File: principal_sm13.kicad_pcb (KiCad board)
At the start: 2 copper layers, 82 parts, among them J1 CN_ARM, J2 CN_POLE, P12 CONN_10X2, P14 SPI, Q1 BC807, Q2 BC807, Q3 BC807, Q4 BC807, U1 L7812, U2 AD8397ARZ, U3 AD8397ARZ, X1 8.192MHz, X2 8.192MHz

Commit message: cambios en el placement
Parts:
- removed the C11 at (63.3, -95.7) (x3)
- removed the C12 at (63.3, -90.8) (x3)
- removed the C2 at (56.5, -71.0)
- removed the R1 at (63.3, -80.9) (x4)
- removed the R3 at (63.3, -85.8) (x3)
- removed the R4 at (63.3, -100.7) (x3)
- removed the U1 at (73.0, -66.5)
- added C27: 0,1µ, Capacitor_SMD:C_1206_3216Metric_Pad1.42x1.75mm_HandSolder, F.Cu at (56.5, -70.5)
- added R7: 1K, Resistor_SMD:R_1206_3216Metric_Pad1.42x1.75mm_HandSolder, F.Cu at (63.3, -80.9)
- added U3: L7812, Package_TO_SOT_THT:TO-218-3_Vertical, F.Cu at (73.0, -66.5)
- moved C13 0.27 mm to (56.5, -75.9)
- moved C7 0.27 mm to (49.0, -75.9)
- moved C12 0.10 mm to (56.5, -80.9)
- moved C6 0.10 mm to (49.0, -80.9)
- moved C19 0.07 mm to (-7.99, -81.1)
- renumbered C11 to C1, C8 to C10, C15 to C11, C9 to C12, C10 to C13, C24 to C14, C25 to C15, C26 to C16, C16 to C17, C19 to C18, C17 to C19, C12 to C2, C18 to C21, C21 to C22, C27 to C23, C22 to C24, C23 to C25, C1 to C26, C14 to C3, C3 to C4, C6 to C5, C4 to C6, C13 to C8, C5 to C9, P12 to P1, P14 to P2, R12 to R1, R11 to R10, R13 to R11, R20 to R12, R5 to R13, R15 to R14, R16 to R15, R17 to R16, R2 to R17, R14 to R18, R18 to R19, R4 to R2, R19 to R20, R6 to R3, R8 to R4, R9 to R5, R3 to R6, R7 to R8, R10 to R9, U2 to U1, U3 to U2

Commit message: componentes montados sobre placa CIAA NXP para hacer el sandwich
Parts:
- added F4: fiducial, Fiducial_1mm_BOT, F.Cu at (237.0, 104.0)
- added F5: fiducial, Fiducial_1mm_BOT, F.Cu at (120.6, 104.0)
- added F6: fiducial, Fiducial_1mm_BOT, F.Cu at (120.6, 180.5)
- P1, P2: moved to B.Cu
- moved J1 293.9 mm to (227.2, 103.9), turned to 180 degrees
- moved J2 293.9 mm to (170.7, 103.9), turned to 180 degrees
- moved P1 288.3 mm to (202.5, 147.7), turned to 270 degrees
- moved P2 282.0 mm to (157.7, 144.4)
- moved C27 276.0 mm to (239.1, 136.5), turned to 180 degrees
- moved C1 269.1 mm to (221.3, 122.1)
- moved C10 269.1 mm to (185.5, 127.3)
- moved C11 269.1 mm to (200.5, 117.3)
- moved C14 269.1 mm to (164.5, 122.1)
- moved C15 269.1 mm to (164.5, 127.0)
- moved C16 269.1 mm to (128.7, 117.3)
- moved C17 269.1 mm to (157.5, 112.3)
- moved C2 269.1 mm to (221.3, 127.0)
- moved C21 269.1 mm to (143.2, 127.3)
- moved C22 269.1 mm to (128.7, 127.3)
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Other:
- board outline added: 138.6 x 86.2 mm
- copper layers 2 -> 4
- net class Default: clearance 0.2 -> 0.2032; trace_width 0.25 -> 0.254; via_dia 0.8 -> 0.635; via_drill 0.4 -> 0.254
- net class POWER-IN added: clearance 0.2032, trace_width 0.762, via_dia 0.635, via_drill 0.254
- net class POWER-OUT added: clearance 0.2032, trace_width 0.508, via_dia 0.635, via_drill 0.254
- net class RS485-CAN added: clearance 0.254, trace_width 0.254, via_dia 0.635, via_drill 0.254
- net class Terminal Block added: clearance 0.2032, trace_width 0.508, via_dia 0.635, via_drill 0.254
- net class USB added: clearance 0.2032, trace_width 0.381, via_dia 0.635, via_drill 0.254
- rule pad_to_mask_clearance: 0 -> 0.0254
- rule trace_clearance: 0.2 -> 0.2032
- rule trace_min: 0.2 -> 0.254
- rule via_min_drill: 0.3 -> 0.254
- rule via_min_size: 0.4 -> 0.635
- board text added: "0 - 1 - 2 - 3 - 4 - 5 - 6 - 7"
- board text added: "1"
- board text added: "AUX"
- board text added: "CI"
- board text added: "CIAA-NXP"
- board text added: "DBG"
- board text added: "DIG. IN→"
- board text added: "DOUT"
- board text added: "DOUT |4|5|6|7|"
- board text added: "OTG"
- board text added: "PWR"
- board text added: "v1.0"
- board text added: "|"
- board text added: "|0|1|2|3|"

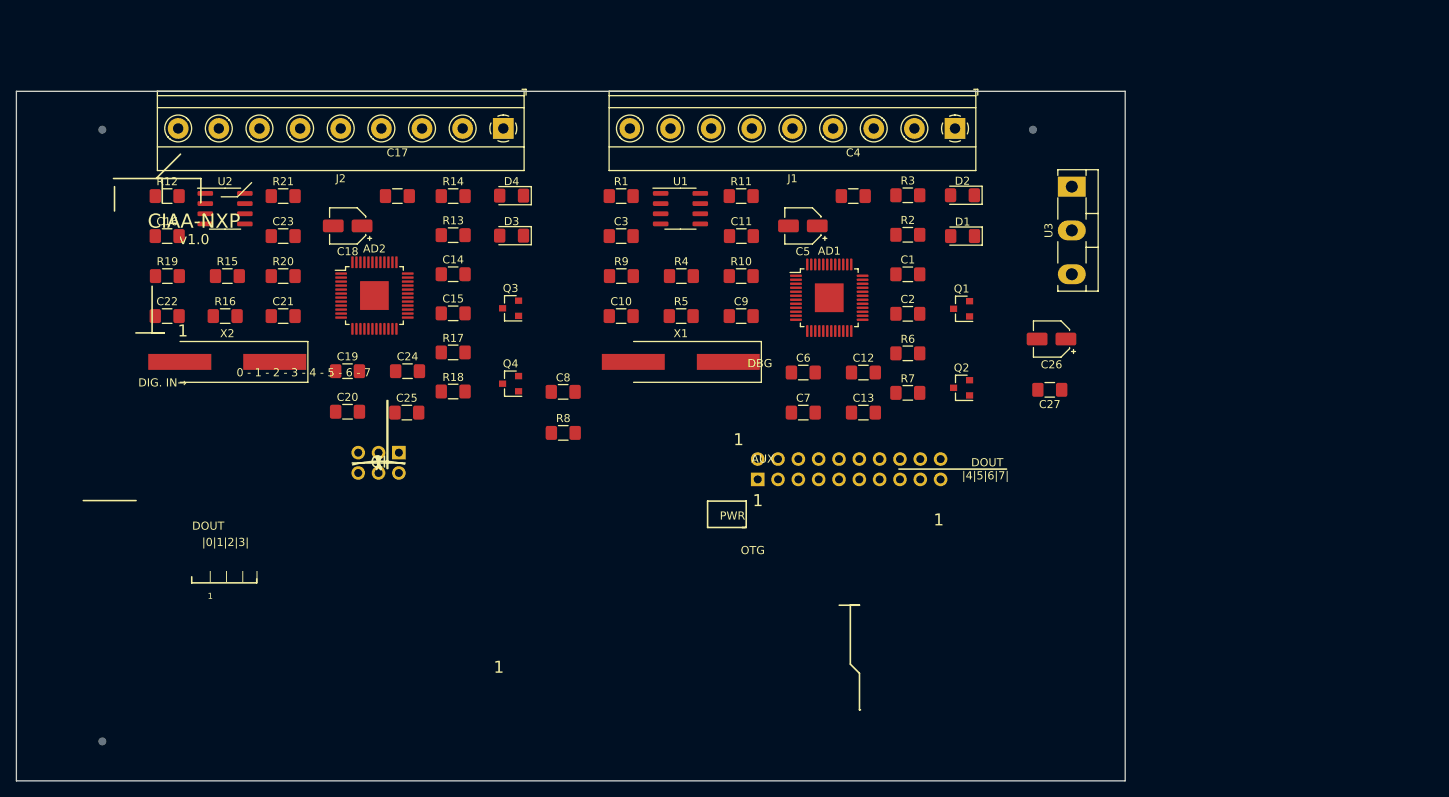
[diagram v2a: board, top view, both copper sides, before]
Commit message: reubicados componentes, cambiado regulador a SMD
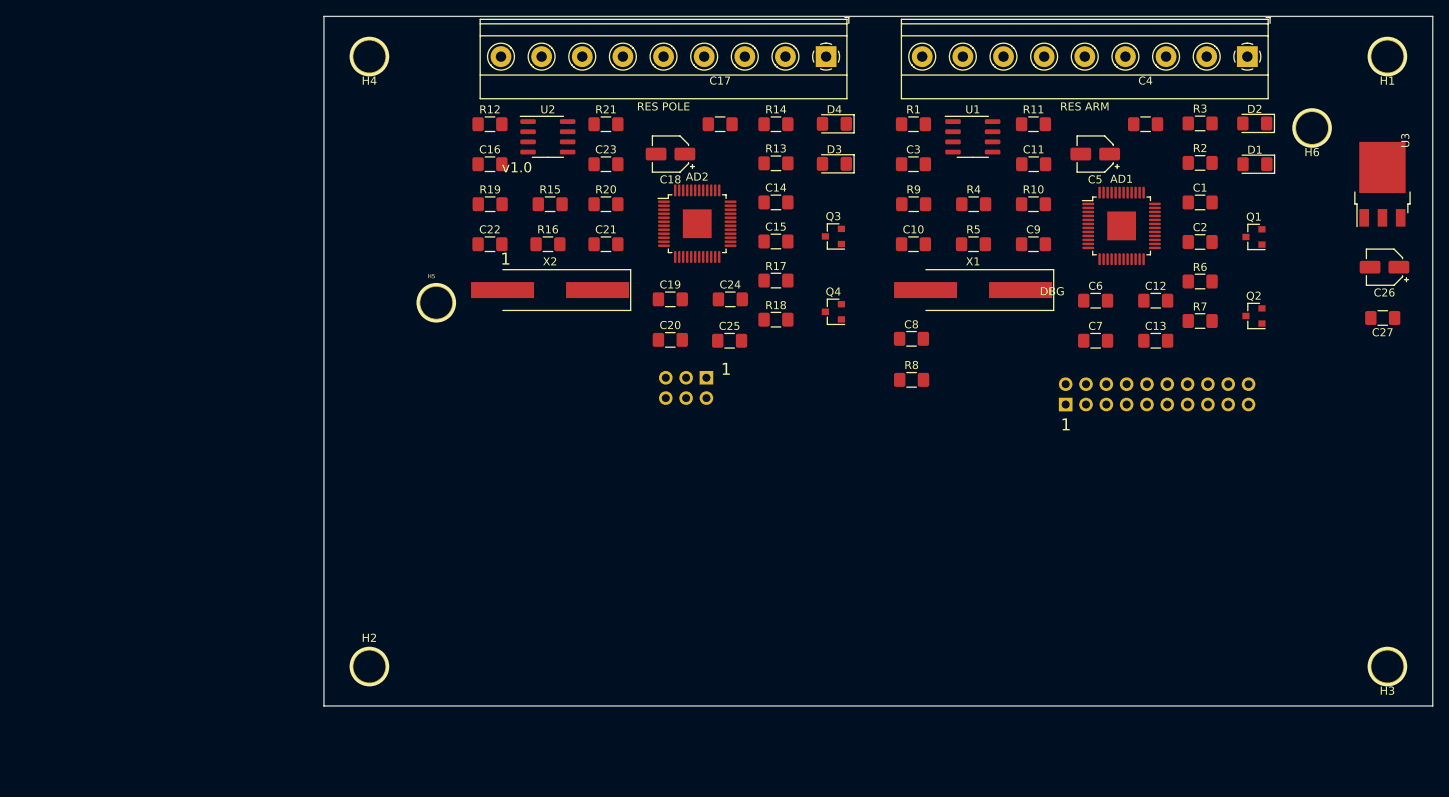
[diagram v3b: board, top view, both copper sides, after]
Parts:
- removed F4, F5, F6: fiducial, Fiducial_1mm_BOT
- removed P2: SPI, Connector_PinSocket_2.54mm:PinSocket_2x03_P2.54mm_Vertical
- added ?: , , F.Cu at (463.9, 242.3)
- added H1: 4mm, 1pin, F.Cu at (281.3, 94.9)
- added H2: 4mm, 1pin, F.Cu at (154.0, 171.1)
- added H3: 4mm, 1pin, F.Cu at (281.3, 171.1)
- added H4: 4mm, 1pin, F.Cu at (154.0, 94.9)
- added H5: 4mm, 1pin, F.Cu at (162.4, 125.6)
- added H6: 4mm, 1pin, F.Cu at (271.8, 103.8)
- added SPI: SPI, Connector_PinSocket_2.54mm:PinSocket_2x03_P2.54mm_Vertical, B.Cu at (196.1, 135.0)
- RES ARM: renamed from J1
- RES POLE: renamed from J2
- U3: footprint Package_TO_SOT_THT:TO-218-3_Vertical -> Package_TO_SOT_SMD:TO-252-3_TabPin2
- moved C8 44.0 mm to (221.8, 130.2)
- moved R8 44.0 mm to (221.8, 135.3)
- moved C27 42.6 mm to (280.7, 127.5)
- moved C26 42.6 mm to (280.9, 121.2)
- moved C17 41.3 mm to (197.9, 103.3)
- moved C25 41.3 mm to (199.0, 130.4)
- moved D3 41.3 mm to (212.1, 108.3)
- moved D4 41.3 mm to (212.1, 103.3)
- moved R15 41.3 mm to (176.6, 113.3)
- moved R19 41.3 mm to (169.1, 113.3)
- moved R18 41.3 mm to (204.8, 127.8)
- moved AD2 41.3 mm to (195.0, 115.8)
- moved C14 41.3 mm to (204.8, 113.1)
- moved C15 41.3 mm to (204.8, 118.0)
- moved C16 41.3 mm to (169.1, 108.3)
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- renumbered P1 to GPIO
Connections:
- AD1 pad 14: Net-(AD1-Pad14) -> (no net)
- AD1 pad 15: Net-(AD1-Pad15) -> (no net)
- AD1 pad 16: Net-(AD1-Pad16) -> (no net)
- AD1 pad 17: Net-(AD1-Pad17) -> (no net)
- AD1 pad 20: Net-(AD1-Pad20) -> (no net)
- AD1 pad 21: Net-(AD1-Pad21) -> (no net)
- AD1 pad 22: Net-(AD1-Pad22) -> (no net)
- AD1 pad 23: Net-(AD1-Pad23) -> (no net)
- AD1 pad 24: Net-(AD1-Pad24) -> (no net)
- AD1 pad 25: Net-(AD1-Pad25) -> (no net)
- AD1 pad 26: Net-(AD1-Pad26) -> (no net)
- AD1 pad 27: Net-(AD1-Pad27) -> (no net)
- AD1 pad 28: Net-(AD1-Pad28) -> (no net)
- AD1 pad 29: Net-(AD1-Pad29) -> (no net)
- AD1 pad 3: Net-(AD1-Pad3) -> (no net)
- AD1 pad 30: Net-(AD1-Pad30) -> (no net)
- AD1 pad 31: Net-(AD1-Pad31) -> (no net)
- AD1 pad 32: Net-(AD1-Pad32) -> (no net)
- AD1 pad 47: Net-(AD1-Pad47) -> (no net)
- AD2 pad 14: Net-(AD2-Pad14) -> (no net)
- AD2 pad 15: Net-(AD2-Pad15) -> (no net)
- AD2 pad 16: Net-(AD2-Pad16) -> (no net)
- AD2 pad 17: Net-(AD2-Pad17) -> (no net)
- AD2 pad 20: Net-(AD2-Pad20) -> (no net)
- AD2 pad 21: Net-(AD2-Pad21) -> (no net)
- AD2 pad 22: Net-(AD2-Pad22) -> (no net)
- AD2 pad 23: Net-(AD2-Pad23) -> (no net)
- AD2 pad 24: Net-(AD2-Pad24) -> (no net)
- AD2 pad 25: Net-(AD2-Pad25) -> (no net)
- AD2 pad 26: Net-(AD2-Pad26) -> (no net)
- AD2 pad 27: Net-(AD2-Pad27) -> (no net)
- AD2 pad 28: Net-(AD2-Pad28) -> (no net)
- AD2 pad 29: Net-(AD2-Pad29) -> (no net)
- AD2 pad 3: Net-(AD2-Pad3) -> (no net)
- AD2 pad 30: Net-(AD2-Pad30) -> (no net)
- AD2 pad 31: Net-(AD2-Pad31) -> (no net)
- AD2 pad 32: Net-(AD2-Pad32) -> (no net)
- AD2 pad 47: Net-(AD2-Pad47) -> (no net)
- GPIO pad 11: /GPIO/GPIO4 -> (no net)
- GPIO pad 12: /GPIO/GPIO5 -> (no net)
- GPIO pad 13: /GPIO/GPIO6 -> (no net)
- GPIO pad 14: /GPIO/GPIO7 -> (no net)
- GPIO pad 15: /GPIO/GPIO8 -> (no net)
- GPIO pad 16: /GPIO/GPIO9 -> (no net)
- GPIO pad 17: /GPIO/GPIO10 -> (no net)
- GPIO pad 18: /GPIO/GPIO11 -> (no net)
- GPIO pad 19: /GPIO/GPIO12 -> (no net)
- GPIO pad 20: /GPIO/GPIO13 -> (no net)
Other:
- copper layers 4 -> 2
- net class Default: trace_width 0.254 -> 0.5; via_drill 0.254 -> 0.5
- net class POWER-IN: via_drill 0.254 -> 0.5
- net class POWER-OUT: via_drill 0.254 -> 0.5
- net class RS485-CAN: trace_width 0.254 -> 0.5; via_drill 0.254 -> 0.5
- net class Terminal Block: via_drill 0.254 -> 0.5
- net class USB: trace_width 0.381 -> 0.5; via_drill 0.254 -> 0.5
- rule trace_min: 0.254 -> 0.5
- rule via_min_drill: 0.254 -> 0.5
- board text removed: "0 - 1 - 2 - 3 - 4 - 5 - 6 - 7"
- board text removed: "AUX"
- board text removed: "CI"
- board text removed: "CIAA-NXP"
- board text removed: "DIG. IN→"
- board text removed: "DOUT"
- board text removed: "DOUT |4|5|6|7|"
- board text removed: "OTG"
- board text removed: "PWR"
- board text removed: "|"
- board text removed: "|0|1|2|3|"

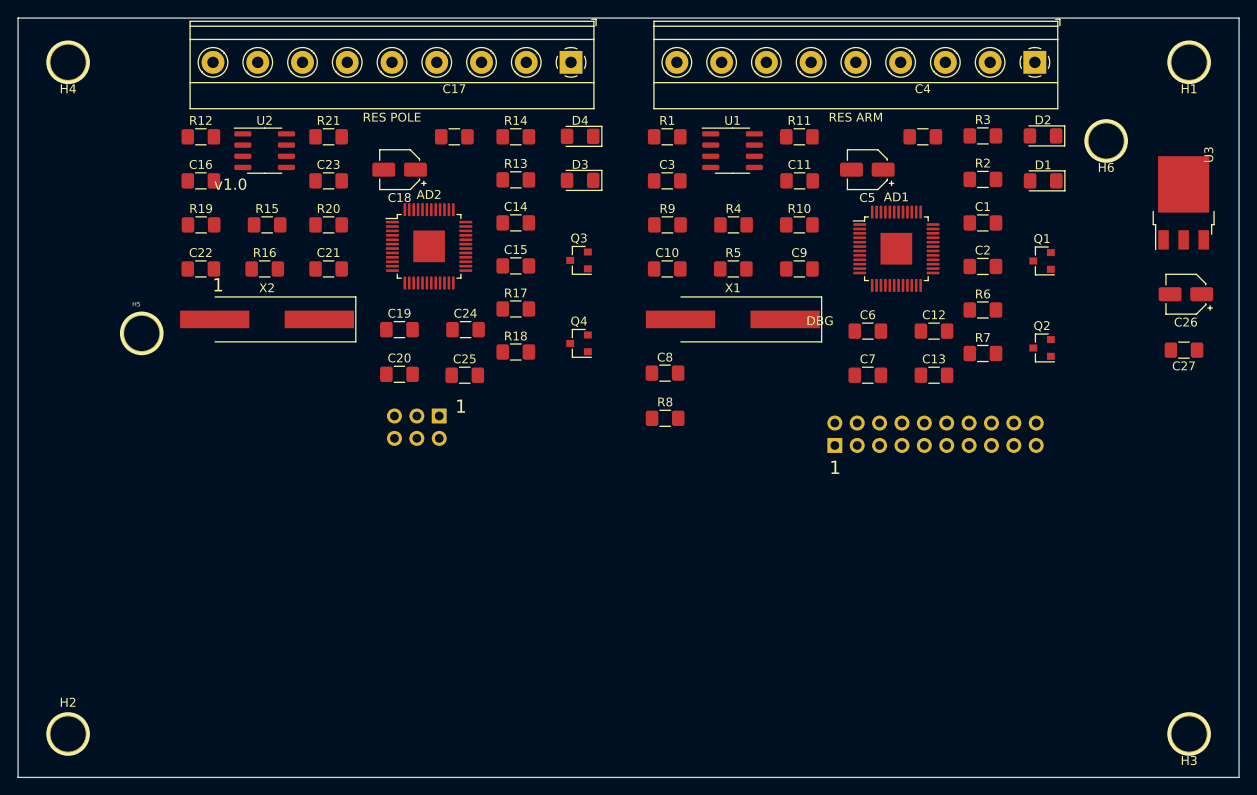
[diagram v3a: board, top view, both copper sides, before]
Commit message: routeado completo, quedan 32 vias
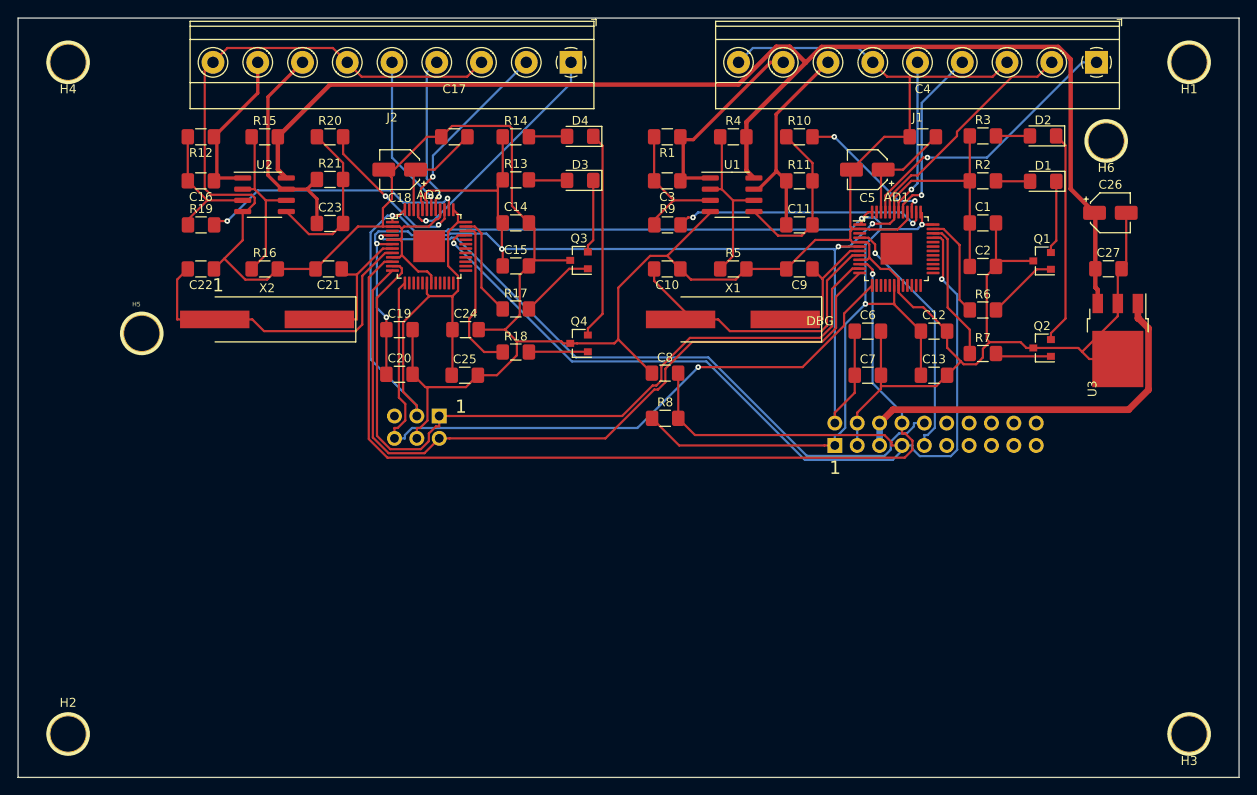
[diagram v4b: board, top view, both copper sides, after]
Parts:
- removed ?: , 
- J1: renamed from RES ARM
- J2: renamed from RES POLE
- moved U3 17.3 mm to (273.2, 126.5), turned to 270 degrees
- moved C27 12.6 mm to (272.1, 118.3), turned to 0 degrees
- moved C26 12.6 mm to (272.3, 112.0), turned to 0 degrees
- moved R15 10.0 mm to (176.3, 103.3)
- moved R20 10.0 mm to (183.7, 103.3)
- moved R4 10.0 mm to (229.5, 103.3)
- moved R10 10.0 mm to (237.0, 103.3)
- moved J1 7.00 mm to (270.7, 94.9)
- moved U1 5.01 mm to (229.4, 109.9)
- moved U2 5.01 mm to (176.3, 109.9)
- moved C11 5.00 mm to (237.0, 113.3)
- moved R11 5.00 mm to (237.0, 108.3)
- moved C23 4.84 mm to (183.7, 113.2)
- moved R21 4.84 mm to (183.7, 108.2)
- moved R2 0.16 mm to (257.8, 108.3)
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- renumbered GPIO to P12, SPI to P14
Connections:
- AD1 pad 14: (no net) -> Net-(AD1-Pad14)
- AD1 pad 15: (no net) -> Net-(AD1-Pad15)
- AD1 pad 16: (no net) -> Net-(AD1-Pad16)
- AD1 pad 17: (no net) -> Net-(AD1-Pad17)
- AD1 pad 20: (no net) -> Net-(AD1-Pad20)
- AD1 pad 21: (no net) -> Net-(AD1-Pad21)
- AD1 pad 22: (no net) -> Net-(AD1-Pad22)
- AD1 pad 23: (no net) -> Net-(AD1-Pad23)
- AD1 pad 24: (no net) -> Net-(AD1-Pad24)
- AD1 pad 25: (no net) -> Net-(AD1-Pad25)
- AD1 pad 26: (no net) -> Net-(AD1-Pad26)
- AD1 pad 27: (no net) -> Net-(AD1-Pad27)
- AD1 pad 28: (no net) -> Net-(AD1-Pad28)
- AD1 pad 29: (no net) -> Net-(AD1-Pad29)
- AD1 pad 3: (no net) -> Net-(AD1-Pad3)
- AD1 pad 30: (no net) -> Net-(AD1-Pad30)
- AD1 pad 31: (no net) -> Net-(AD1-Pad31)
- AD1 pad 32: (no net) -> Net-(AD1-Pad32)
- AD1 pad 47: (no net) -> Net-(AD1-Pad47)
- AD2 pad 14: (no net) -> Net-(AD2-Pad14)
- AD2 pad 15: (no net) -> Net-(AD2-Pad15)
- AD2 pad 16: (no net) -> Net-(AD2-Pad16)
- AD2 pad 17: (no net) -> Net-(AD2-Pad17)
- AD2 pad 20: (no net) -> Net-(AD2-Pad20)
- AD2 pad 21: (no net) -> Net-(AD2-Pad21)
- AD2 pad 22: (no net) -> Net-(AD2-Pad22)
- AD2 pad 23: (no net) -> Net-(AD2-Pad23)
- AD2 pad 24: (no net) -> Net-(AD2-Pad24)
- AD2 pad 25: (no net) -> Net-(AD2-Pad25)
- AD2 pad 26: (no net) -> Net-(AD2-Pad26)
- AD2 pad 27: (no net) -> Net-(AD2-Pad27)
- AD2 pad 28: (no net) -> Net-(AD2-Pad28)
- AD2 pad 29: (no net) -> Net-(AD2-Pad29)
- AD2 pad 3: (no net) -> Net-(AD2-Pad3)
- AD2 pad 30: (no net) -> Net-(AD2-Pad30)
- AD2 pad 31: (no net) -> Net-(AD2-Pad31)
- AD2 pad 32: (no net) -> Net-(AD2-Pad32)
- AD2 pad 47: (no net) -> Net-(AD2-Pad47)
- J1 pad 1: Net-(C3-Pad1) -> /RDC ARM/COS
- J1 pad 2: Net-(C11-Pad1) -> /RDC ARM/COSLO
- J1 pad 7: /RDC ARM/COS -> Net-(C11-Pad1)
- J1 pad 8: /RDC ARM/COSLO -> Net-(C3-Pad1)
- J2 pad 1: Net-(C16-Pad1) -> /RDC POLE/COS
- J2 pad 2: Net-(C23-Pad1) -> /RDC POLE/COSLO
- J2 pad 7: /RDC POLE/COS -> Net-(C23-Pad1)
- J2 pad 8: /RDC POLE/COSLO -> Net-(C16-Pad1)
- P12 pad 11: (no net) -> /GPIO/GPIO4
- P12 pad 12: (no net) -> /GPIO/GPIO5
- P12 pad 13: (no net) -> /GPIO/GPIO6
- P12 pad 14: (no net) -> /GPIO/GPIO7
- P12 pad 15: (no net) -> /GPIO/GPIO8
- P12 pad 16: (no net) -> /GPIO/GPIO9
- P12 pad 17: (no net) -> /GPIO/GPIO10
- P12 pad 18: (no net) -> /GPIO/GPIO11
- P12 pad 19: (no net) -> /GPIO/GPIO12
- P12 pad 20: (no net) -> /GPIO/GPIO13
- P14 pad 5: (no net) -> /GPIO/SPI_CS
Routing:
- net GND: track 0.00 -> 417.2 mm
- net +3V3: track 0.00 -> 200.8 mm, vias 0 -> 4
- net +5V: track 0.00 -> 165.3 mm, vias 0 -> 5
- net +12V: track 0.00 -> 146.6 mm
- net /GPIO/GPIO0: track 0.00 -> 129.4 mm, vias 0 -> 2
- net /GPIO/GPIO1: track 0.00 -> 109.0 mm, vias 0 -> 1
- net /RDC ARM/MISO: track 0.00 -> 89.9 mm
- net /RDC ARM/MOSI: track 0.00 -> 87.3 mm
- net /GPIO/SPI_SCK: track 0.00 -> 81.4 mm, vias 0 -> 1
- net /GPIO/GPIO3: track 0.00 -> 75.8 mm, vias 0 -> 1
- net +24V: track 0.00 -> 45.0 mm
- net Net-(AD2-Pad8): track 0.00 -> 38.1 mm
- net Net-(AD1-Pad8): track 0.00 -> 35.0 mm
- net /RDC ARM/COS: track 0.00 -> 32.1 mm, vias 0 -> 1
- net /RDC POLE/EXC: track 0.00 -> 30.2 mm, vias 0 -> 2
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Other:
- net class Default: trace_width 0.5 -> 0.254; via_drill 0.5 -> 0.254
- net class POWER-IN: via_drill 0.5 -> 0.254
- net class POWER-OUT: via_drill 0.5 -> 0.254
- net class RS485-CAN removed
- net class SALIDAS added: clearance 0.2032, trace_width 0.381, via_dia 0.635, via_drill 0.254
- net class Terminal Block: via_drill 0.5 -> 0.254
- net class USB removed
- rule trace_min: 0.5 -> 0.254
- rule via_min_drill: 0.5 -> 0.254
- board text removed: "v1.0"
